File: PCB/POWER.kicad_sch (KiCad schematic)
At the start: 23 parts, among them U1 OPA1644AxD, U2 OPA1612AxD, U3 LTC3265xDHC

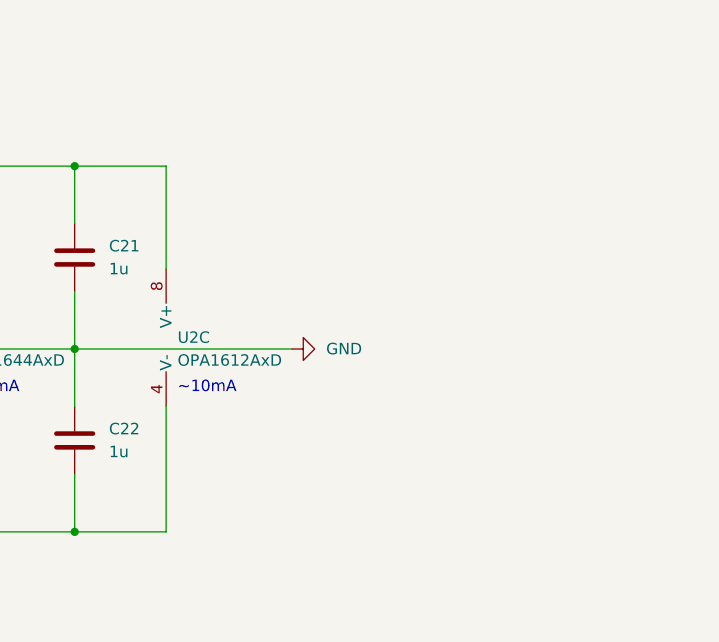
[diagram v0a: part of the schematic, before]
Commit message: differential amp initial changes
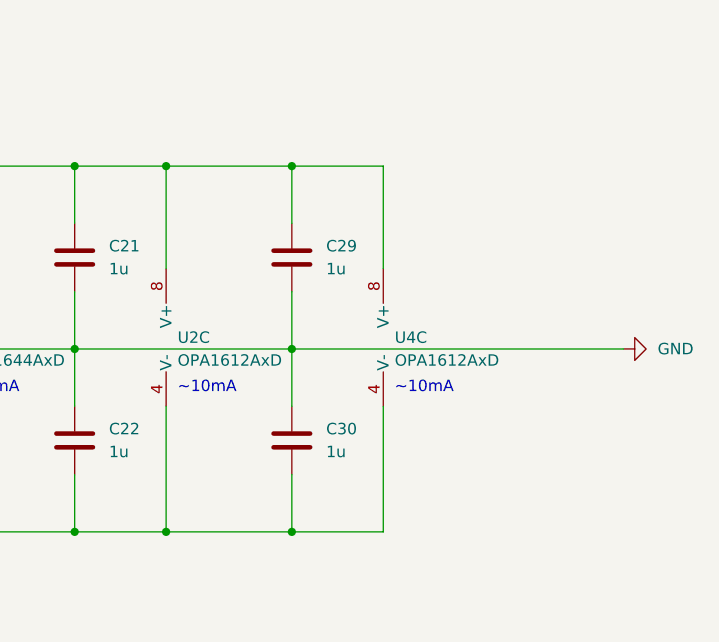
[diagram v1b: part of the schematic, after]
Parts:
- added C29, C30: 1u, Capacitor_SMD:C_0402_1005Metric, symbol Device:C
- added U4: OPA1612AxD, Package_SO:SOIC-8_3.9x4.9mm_P1.27mm, symbol Amplifier_Operational:OPA1612AxD
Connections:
- net +6V: now also C29.2, U4.8 (V+)
- net -6V: now also C30.1, U4.4 (V-)
- net GND: now also C29.1, C30.2
